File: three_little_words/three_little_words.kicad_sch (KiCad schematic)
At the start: 62 parts, among them J1 Eurorack_Power, Q1 2N3904, Q2 2N3904, Q3 2N3904, U1 NE5532, U2 NE5532, U3 NE5532, U4 LM1117-3.3, U5 Pico, U6 L7805

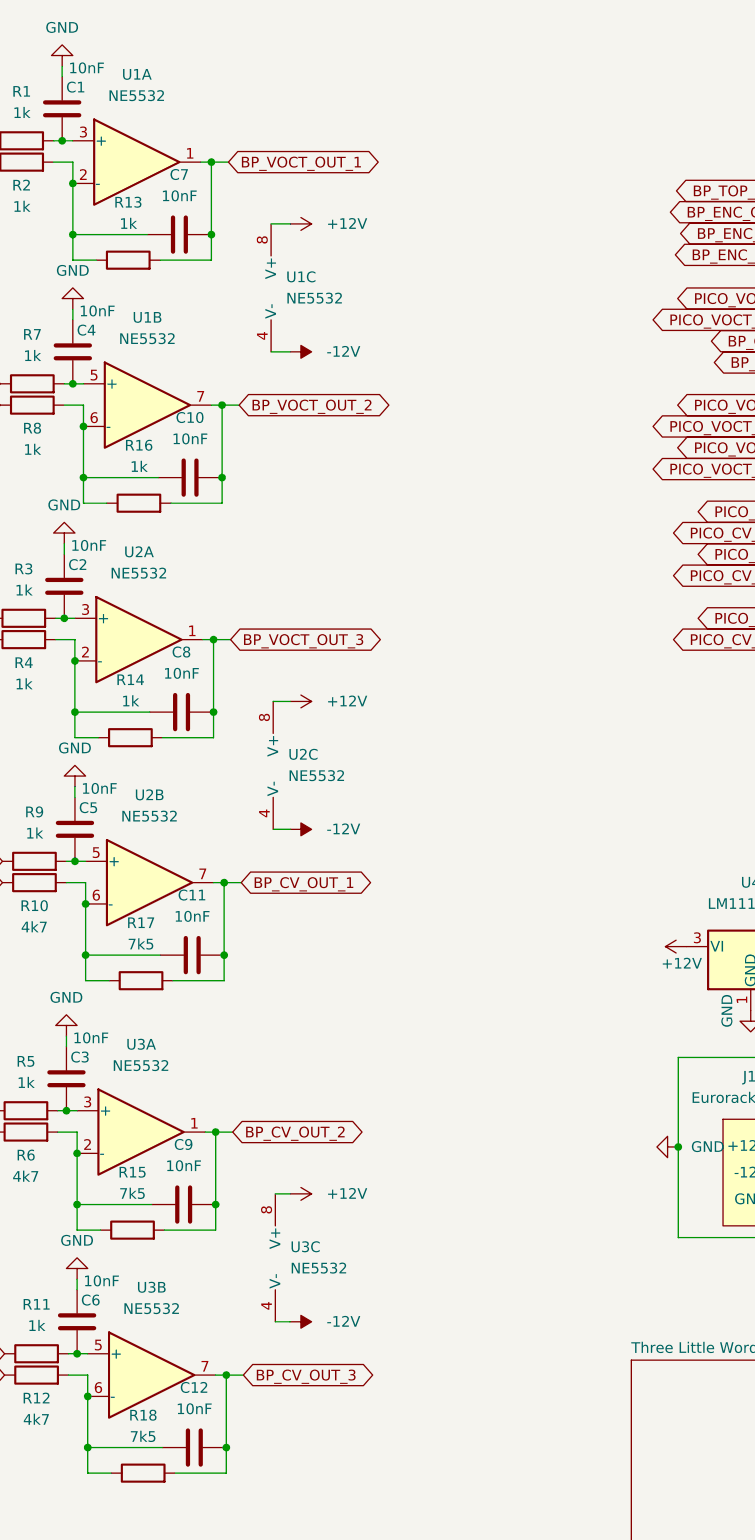
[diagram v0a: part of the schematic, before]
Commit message: Adding 220ohm resistors to outputs
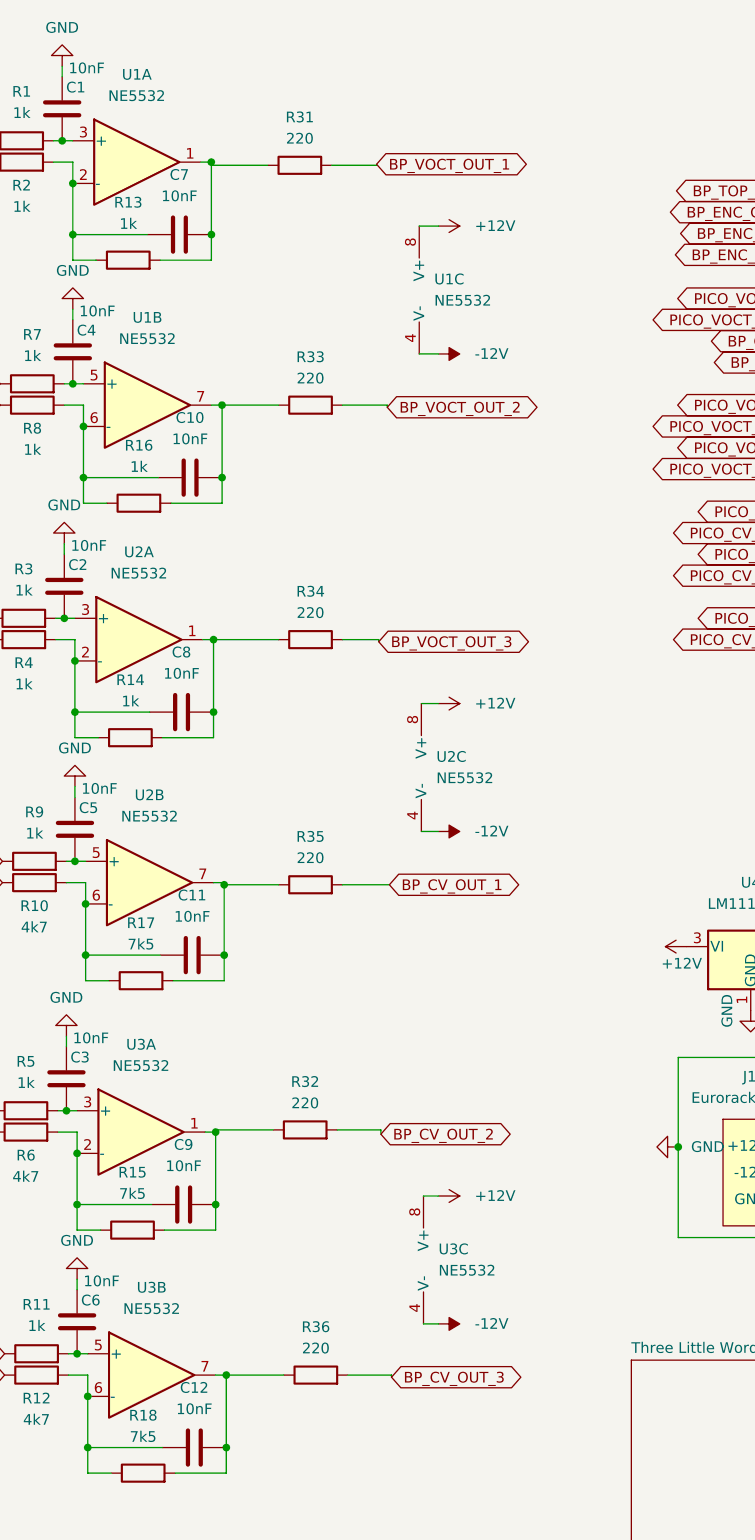
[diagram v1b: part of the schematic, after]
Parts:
- added R31, R32, R33, R34, R35, R36: 220, symbol Device:R
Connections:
- net BP_CV_OUT_1: now also R35.2; no longer C11.2, R17.2, U2.7
- net BP_CV_OUT_2: now also R32.2; no longer C9.2, R15.2, U3.1
- net BP_CV_OUT_3: now also R36.2; no longer C12.2, R18.2, U3.7
- net BP_VOCT_OUT_1: now also R31.2; no longer C7.2, R13.2, U1.1
- net BP_VOCT_OUT_2: now also R33.2; no longer C10.2, R16.2, U1.7
- net BP_VOCT_OUT_3: now also R34.2; no longer C8.2, R14.2, U2.1
- new net: C12.2, R18.2, R36.1, U3.7
- new net: C10.2, R16.2, R33.1, U1.7
- new net: C11.2, R17.2, R35.1, U2.7
- new net: C7.2, R13.2, R31.1, U1.1
- new net: C9.2, R15.2, R32.1, U3.1
- new net: C8.2, R14.2, R34.1, U2.1
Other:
- moved on the sheet: U1C, U2C, U3C

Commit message: Adding footprints for various components of 3lw.
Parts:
- C1, C10, C11, C12, C2, C3, C4, C5, C6, C7, C8, C9: footprint (none) -> Capacitor_THT:C_Disc_D8.0mm_W2.5mm_P5.00mm
- R1, R10, R11, R12, R13, R14, R15, R16, R17, R18, R19, R2, R20, R21, R22, R23, R24, R25, R26, R27, R28, R29, R3, R30, R31, R32, R33, R34, R35, R36, R4, R5, R6, R7, R8, R9: footprint (none) -> Resistor_THT:R_Axial_DIN0207_L6.3mm_D2.5mm_P7.62mm_Horizontal

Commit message: Adding BOM, footprints, starting circuit.
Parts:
- D3, D4, D5, D6, D7, D8: footprint (none) -> Diode_THT:D_DO-35_SOD27_P7.62mm_Horizontal
- U1, U2, U3: footprint (none) -> Package_DIP:DIP-8_W7.62mm
- U5: footprint RPi_Pico:RPi_Pico_SMD_TH -> MCU_RaspberryPi_and_Boards:RPi_Pico_SMD_TH
- U6: footprint (none) -> Package_TO_SOT_THT:TO-220-3_Vertical

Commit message: Tried to sort circuit. Mixed success.
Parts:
- U4: footprint Package_TO_SOT_SMD:SOT-223-3_TabPin2 -> Package_TO_SOT_THT:TO-220-3_Vertical
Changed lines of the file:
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@@
     (property "Reference" "U4" (id 0) (at 126.746 115.316 0))
     (property "Value" "LM1117-3.3" (id 1) (at 126.746 117.856 0))
-    (property "Footprint" "Package_TO_SOT_SMD:SOT-223-3_TabPin2" (id 2) (at 126.746 110.871 0)
+    (property "Footprint" "Package_TO_SOT_THT:TO-220-3_Vertical" (id 2) (at 126.746 110.871 0)
       (effects (font (size 1.27 1.27)) hide)
     )
@@
     )
     (path "/5981d953-5498-4062-b4cd-933f794f0a13/064527ab-1b88-439a-b7a6-ecfa330b715a"
-      (reference "J15") (unit 1) (value "Conn_01x17_Female") (footprint "Connector_PinSocket_2.54mm:PinSocket_1x17_P2.54mm_Vertical")
+      (reference "J15") (unit 1) (value "Conn_01x14_Female") (footprint "Connector_PinSocket_2.54mm:PinSocket_1x14_P2.54mm_Vertical")
     )
     (path "/5981d953-5498-4062-b4cd-933f794f0a13/66fc7aba-df2f-4319-860b-d967c2d72e88"
@@
     )
     (path "/5981d953-5498-4062-b4cd-933f794f0a13/1a9c8dc5-fa51-4297-9bc4-36bcbe891c68"
-      (reference "J17") (unit 1) (value "Conn_01x17_Male") (footprint "Connector_PinHeader_2.54mm:PinHeader_1x17_P2.54mm_Vertical")
+      (reference "J17") (unit 1) (value "Conn_01x14_Male") (footprint "Connector_PinHeader_2.54mm:PinHeader_1x14_P2.54mm_Vertical")
     )
     (path "/5981d953-5498-4062-b4cd-933f794f0a13/aa0ff302-7bf9-4742-941d-932f03772977"
@@
     )
     (path "/eba5d6a9-13c8-47c5-a121-bbcc601465b8"
-      (reference "U4") (unit 1) (value "LM1117-3.3") (footprint "Package_TO_SOT_SMD:SOT-223-3_TabPin2")
+      (reference "U4") (unit 1) (value "LM1117-3.3") (footprint "Package_TO_SOT_THT:TO-220-3_Vertical")
     )
     (path "/7c4b8d5d-82e5-4d8e-b466-275209dde4d0"

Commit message: Finishing 3lw schematic
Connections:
- net BP_GND is gone; now on net GND: U5.38 (GND)
- net +3V3: now also U5.35 (ADC_VREF)
- no-connect marks 15 -> 14
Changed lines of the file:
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@@
   (no_connect (at 158.115 91.44))
   (no_connect (at 137.795 55.88))
-  (no_connect (at 173.355 50.8))
   (no_connect (at 173.355 45.72))
   (no_connect (at 137.795 81.28))
@@
     (stroke (width 0) (type default) (color 0 0 0 0))
   )
+  (wire (pts (xy 192.278 29.464) (xy 194.056 29.464))
+    (stroke (width 0) (type default) (color 0 0 0 0))
+  )
   (wire (pts (xy 46.228 112.776) (xy 47.498 112.776))
     (stroke (width 0) (type default) (color 0 0 0 0))
@@
     )
   )
+  (global_label "BP_GND" (shape bidirectional) (at 192.278 29.464 180) (fields_autoplaced)
+    (effects (font (size 1.27 1.27)) (justify right))
+    (property "Intersheet References" "${INTERSHEET_REFS}" (id 0) (at 182.4868 29.3846 0)
+      (effects (font (size 1.27 1.27)) (justify right) hide)
+    )
+  )
   (global_label "BP_CV_IN_JACK_2" (shape bidirectional) (at 247.396 61.722 180) (fields_autoplaced)
     (effects (font (size 1.27 1.27)) (justify right))
@@
     (effects (font (size 1.27 1.27)) (justify left))
     (property "Intersheet References" "${INTERSHEET_REFS}" (id 0) (at 188.6495 53.2606 0)
+      (effects (font (size 1.27 1.27)) (justify left) hide)
+    )
+  )
+  (global_label "BP_3V3" (shape bidirectional) (at 173.355 50.8 0) (fields_autoplaced)
+    (effects (font (size 1.27 1.27)) (justify left))
+    (property "Intersheet References" "${INTERSHEET_REFS}" (id 0) (at 182.7833 50.8794 0)
       (effects (font (size 1.27 1.27)) (justify left) hide)
     )
@@
     (pin "3")
   )
+  (symbol (lib_id "power:GND") (at 194.056 29.464 90) (unit 1)
+    (in_bom yes) (on_board yes) (fields_autoplaced)
+    (property "Reference" "#PWR01" (id 0) (at 200.406 29.464 0)
+      (effects (font (size 1.27 1.27)) hide)
+    )
+    (property "Value" "GND" (id 1) (at 198.12 29.4639 90)
+      (effects (font (size 1.27 1.27)) (justify right))
+    )
+    (property "Footprint" "" (id 2) (at 194.056 29.464 0)
+      (effects (font (size 1.27 1.27)) hide)
+    )
+    (property "Datasheet" "" (id 3) (at 194.056 29.464 0)
+      (effects (font (size 1.27 1.27)) hide)
+    )
+    (pin "1")
+  )
   (symbol (lib_id "Transistor_BJT:2N3904") (at 242.316 108.204 0) (unit 1)
     (in_bom yes) (on_board yes) (fields_autoplaced)
@@
       (reference "#FLG0102") (unit 1) (value "PWR_FLAG") (footprint "")
     )
+    (path "/d0d946ad-e222-4539-aa2f-ce0d7f96cf16"
+      (reference "#PWR01") (unit 1) (value "GND") (footprint "")
+    )
     (path "/aa5f770f-5510-40f6-a180-6537615b3284"
